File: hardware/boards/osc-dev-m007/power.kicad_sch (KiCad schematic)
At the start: 13 parts, among them J901 JST-PH-H, J902 TERM

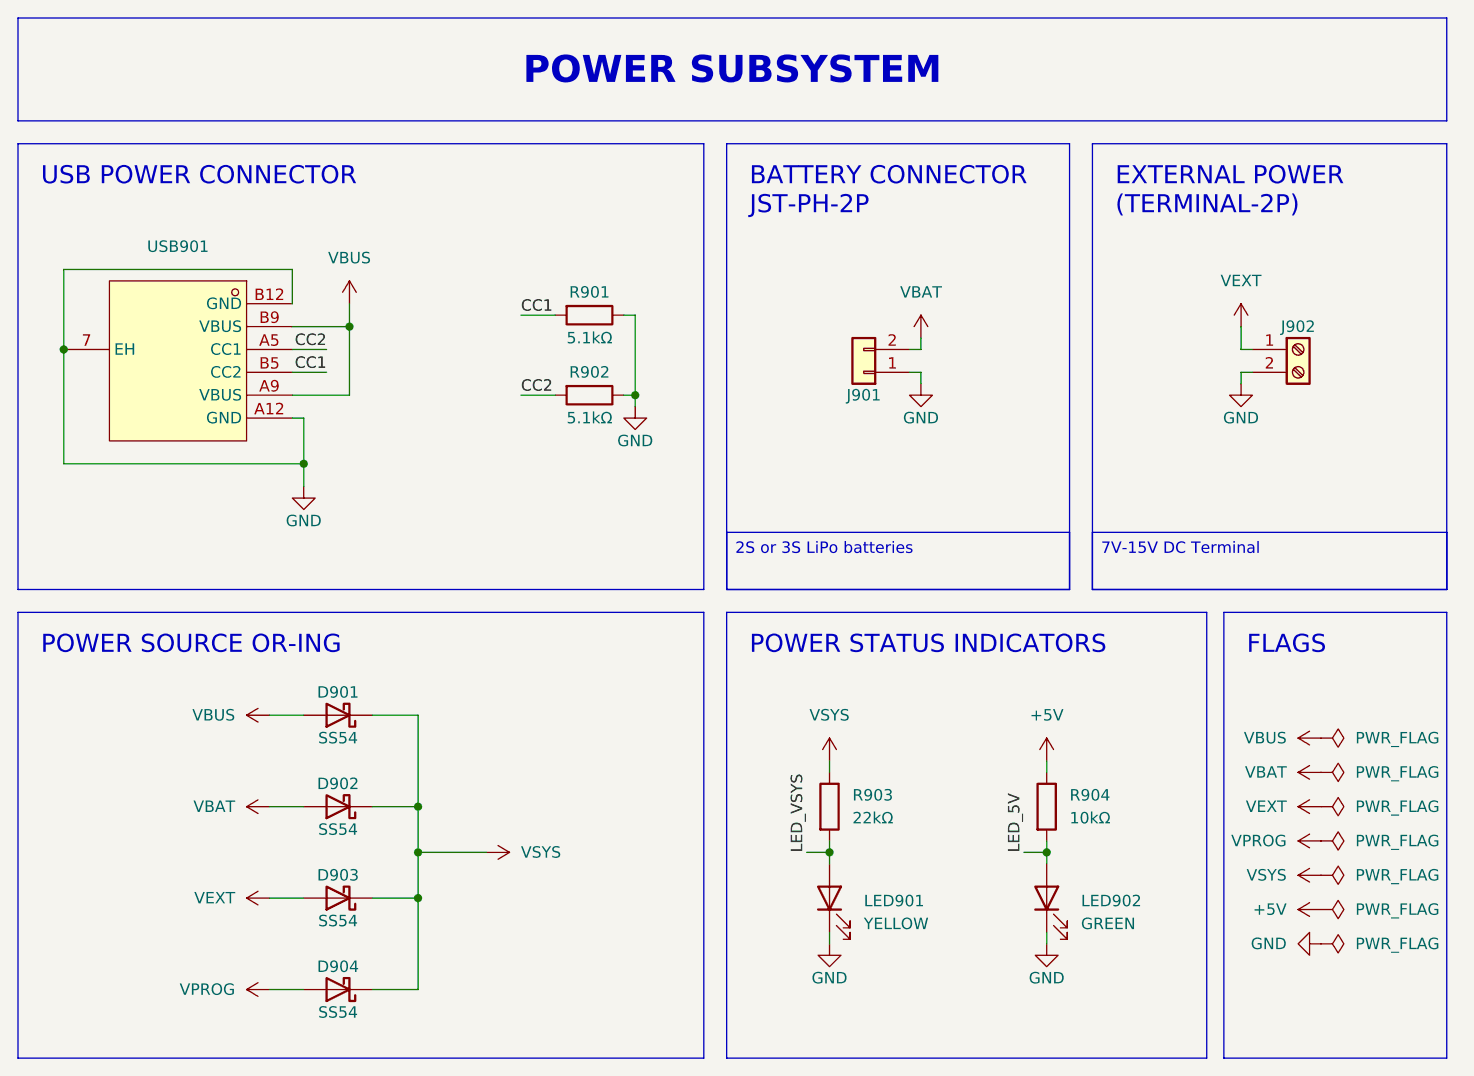
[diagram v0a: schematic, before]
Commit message: hw: design osc-dev-m007 pcb
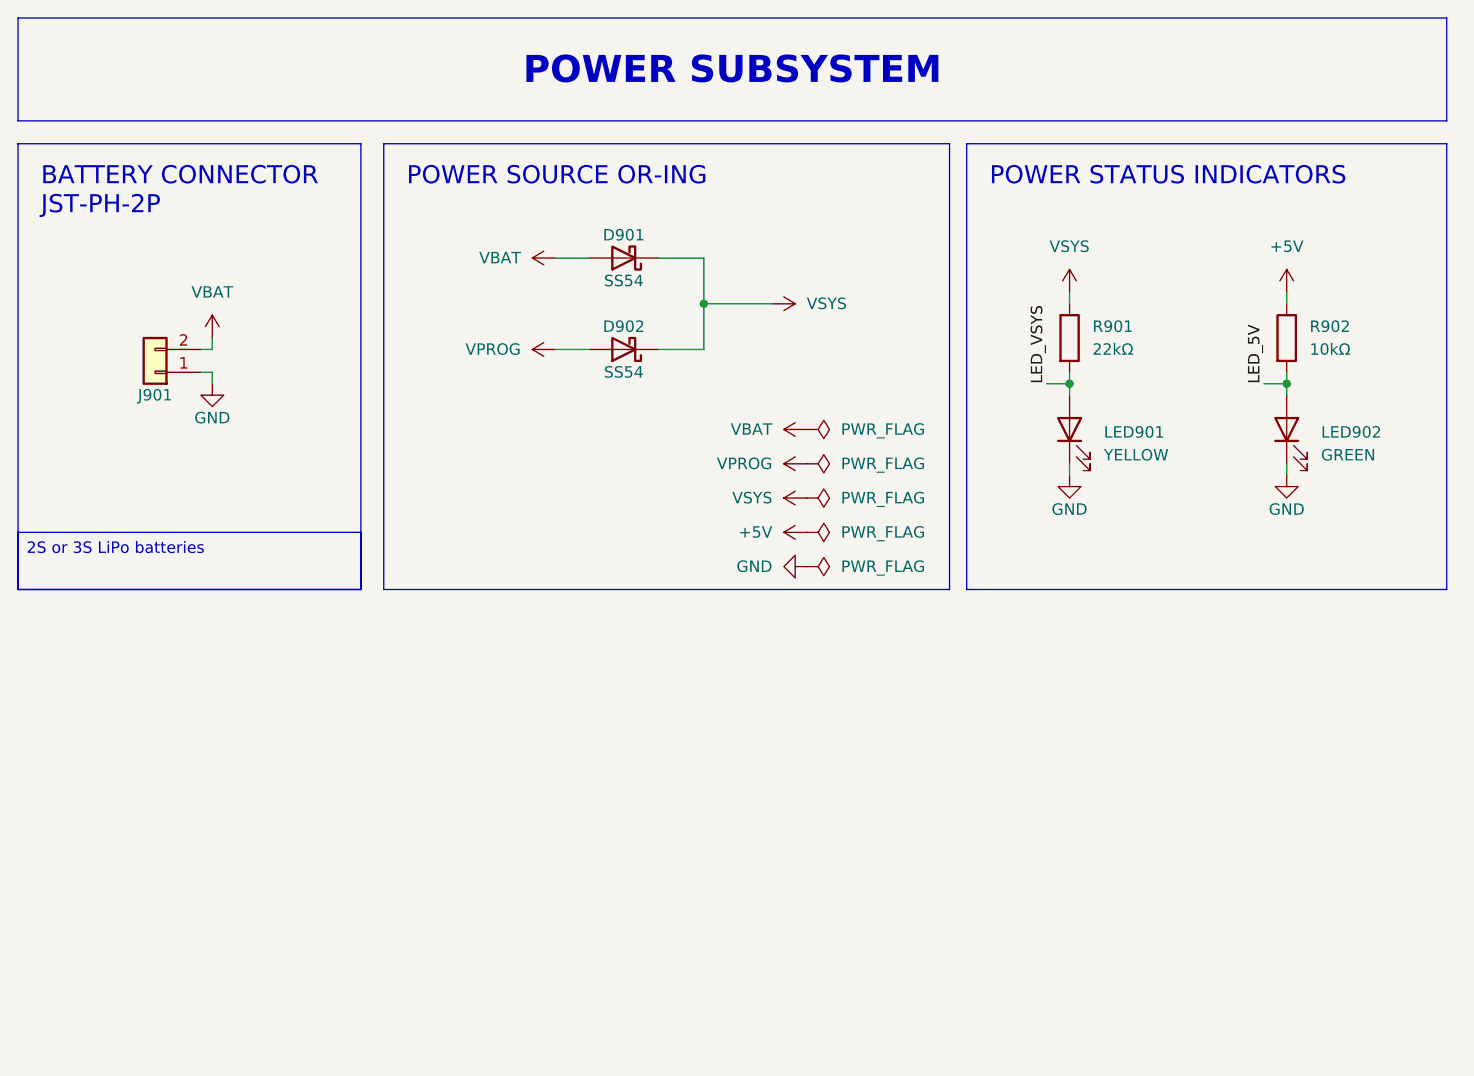
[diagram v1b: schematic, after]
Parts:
- removed D901, D903: SS54, Diode_SMD:D_SMA_Handsoldering, symbol Diode:SS34
- removed J902: TERM, shared:CONN-TH_2P-P5.00_WJ500V-5.08-2P, symbol Connector:Screw_Terminal_01x02
- removed R901, R902: 5.1kΩ, Resistor_SMD:R_0805_2012Metric_Pad1.20x1.40mm_HandSolder, symbol Device:R
- removed USB901: TYPE-C-H, shared:TYPE-C-SMD_TYPE-C-6P-073, symbol shared:TYPE-C6P(073)
- renumbered D902 to D901, D904 to D902, R903 to R901, R904 to R902
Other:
- note removed: "EXTERNAL POWER (TERMINAL-2P)"
- note removed: "FLAGS"
- note removed: "USB POWER CONNECTOR"
- moved on the sheet: D901, D902, J901, LED901, LED902, R901, R902

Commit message: hw: add osc-sg90-m007 renders to readme
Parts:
- R901: value 22kΩ -> 22k
- R902: value 10kΩ -> 10k
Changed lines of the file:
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@@
 			)
 		)
-		(property "Value" "10kΩ"
+		(property "Value" "10k"
 			(at 157.48 50.7999 0)
 			(show_name no)
@@
 			)
 		)
-		(property "Value" "22kΩ"
+		(property "Value" "22k"
 			(at 133.35 50.7999 0)
 			(show_name no)

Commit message: hw: swap dev-m007 parts to in-stock equivalents
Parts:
- R902: LCSC C17414 -> C2907219; MFPN 0805W8F1002T5E -> FRC0805F1002TS
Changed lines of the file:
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@@
 			)
 		)
-		(property "Datasheet" "https://www.lcsc.com/product-detail/C17414.html"
+		(property "Datasheet" "https://www.lcsc.com/product-detail/C2907219.html"
 			(at 154.94 49.53 0)
 			(hide yes)
@@
 			)
 		)
-		(property "LCSC" "C17414"
+		(property "LCSC" "C2907219"
 			(at 157.48 48.2599 0)
 			(hide yes)
@@
 			)
 		)
-		(property "MFPN" "0805W8F1002T5E"
+		(property "MFPN" "FRC0805F1002TS"
 			(at 157.48 48.2599 0)
 			(hide yes)
